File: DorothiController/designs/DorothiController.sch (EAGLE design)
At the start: 25 parts

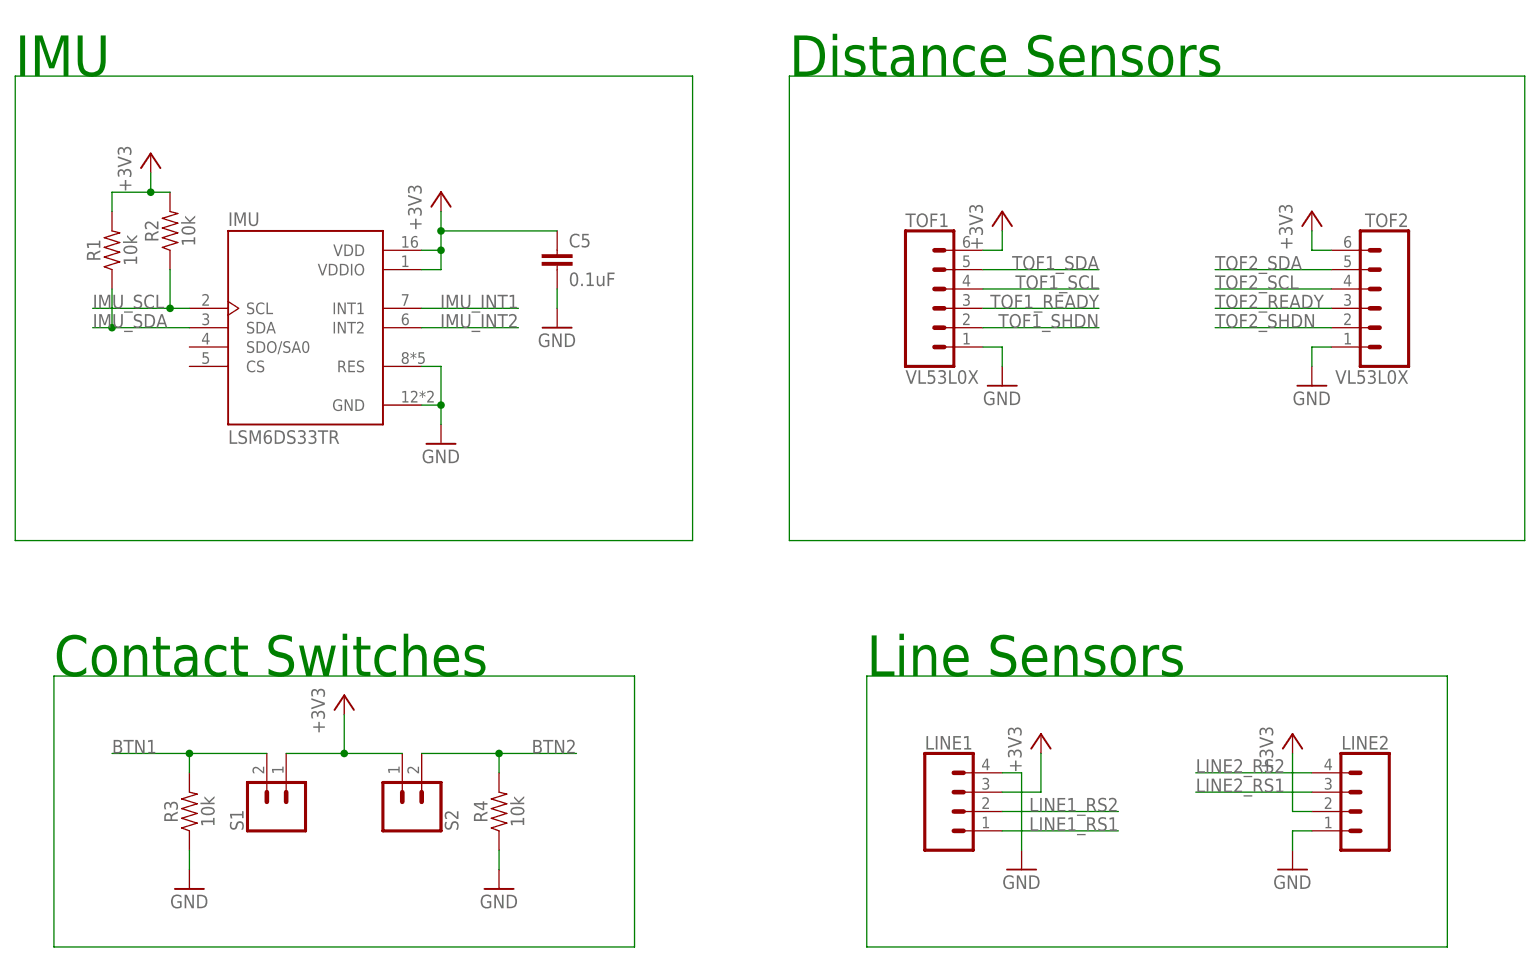
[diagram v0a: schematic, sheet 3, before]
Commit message: silk screen and status diode added
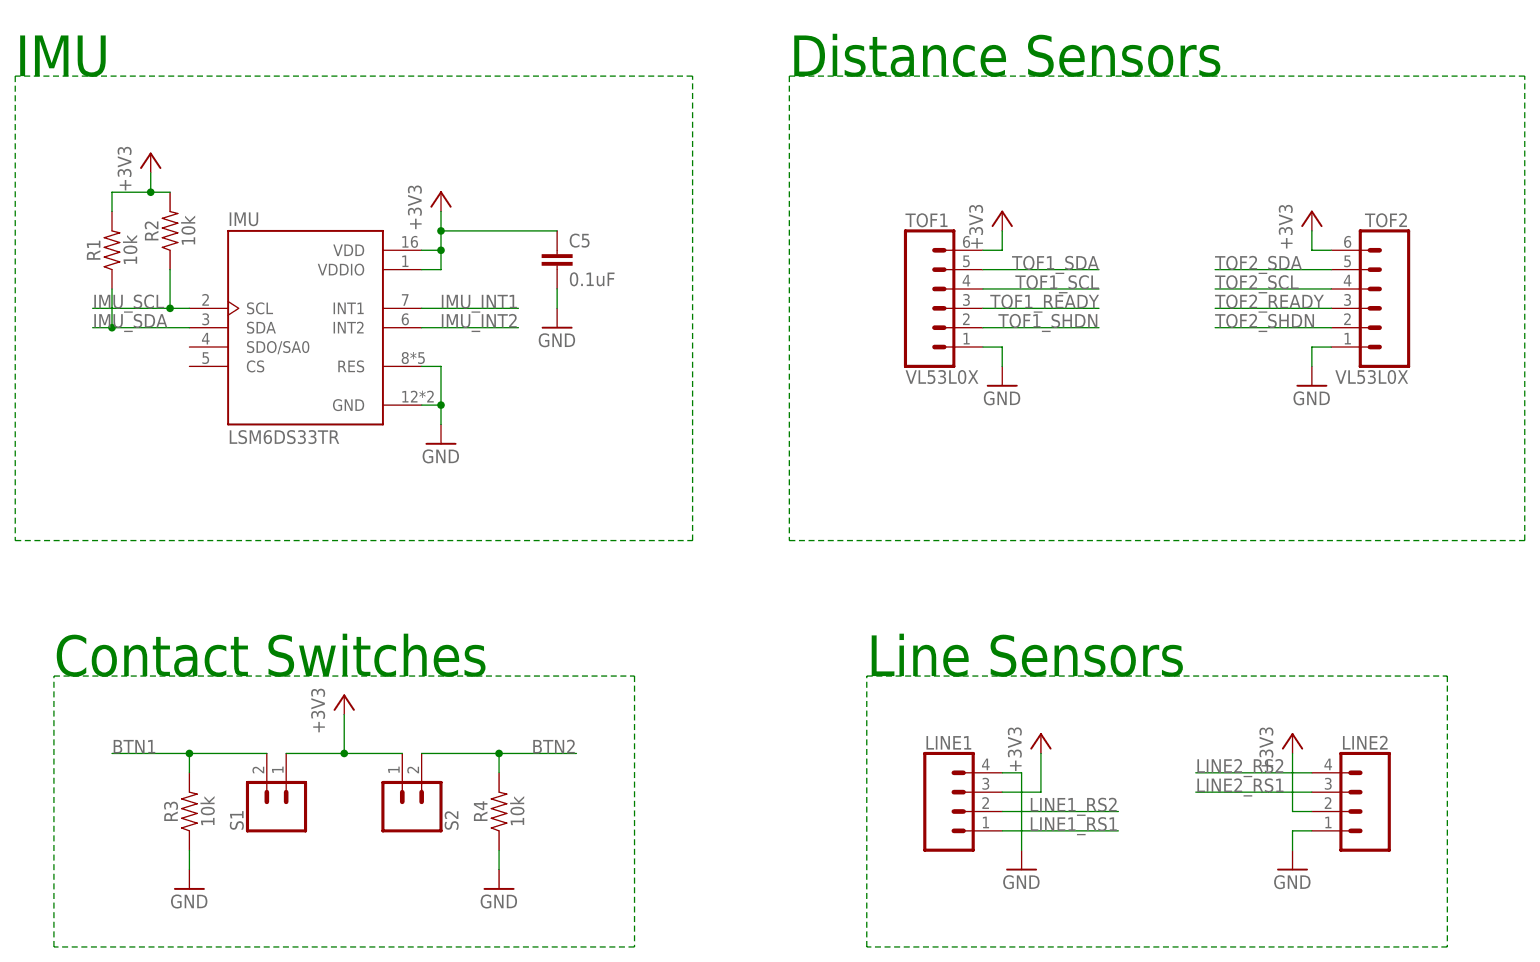
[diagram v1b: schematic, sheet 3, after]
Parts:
- added D1: (no value), SparkFun-LED:LED0603
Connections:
- new net INDICATOR: D1.A, U$1.23/A9/T/PWM
- net GND: now also D1.C

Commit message: forgot resistor
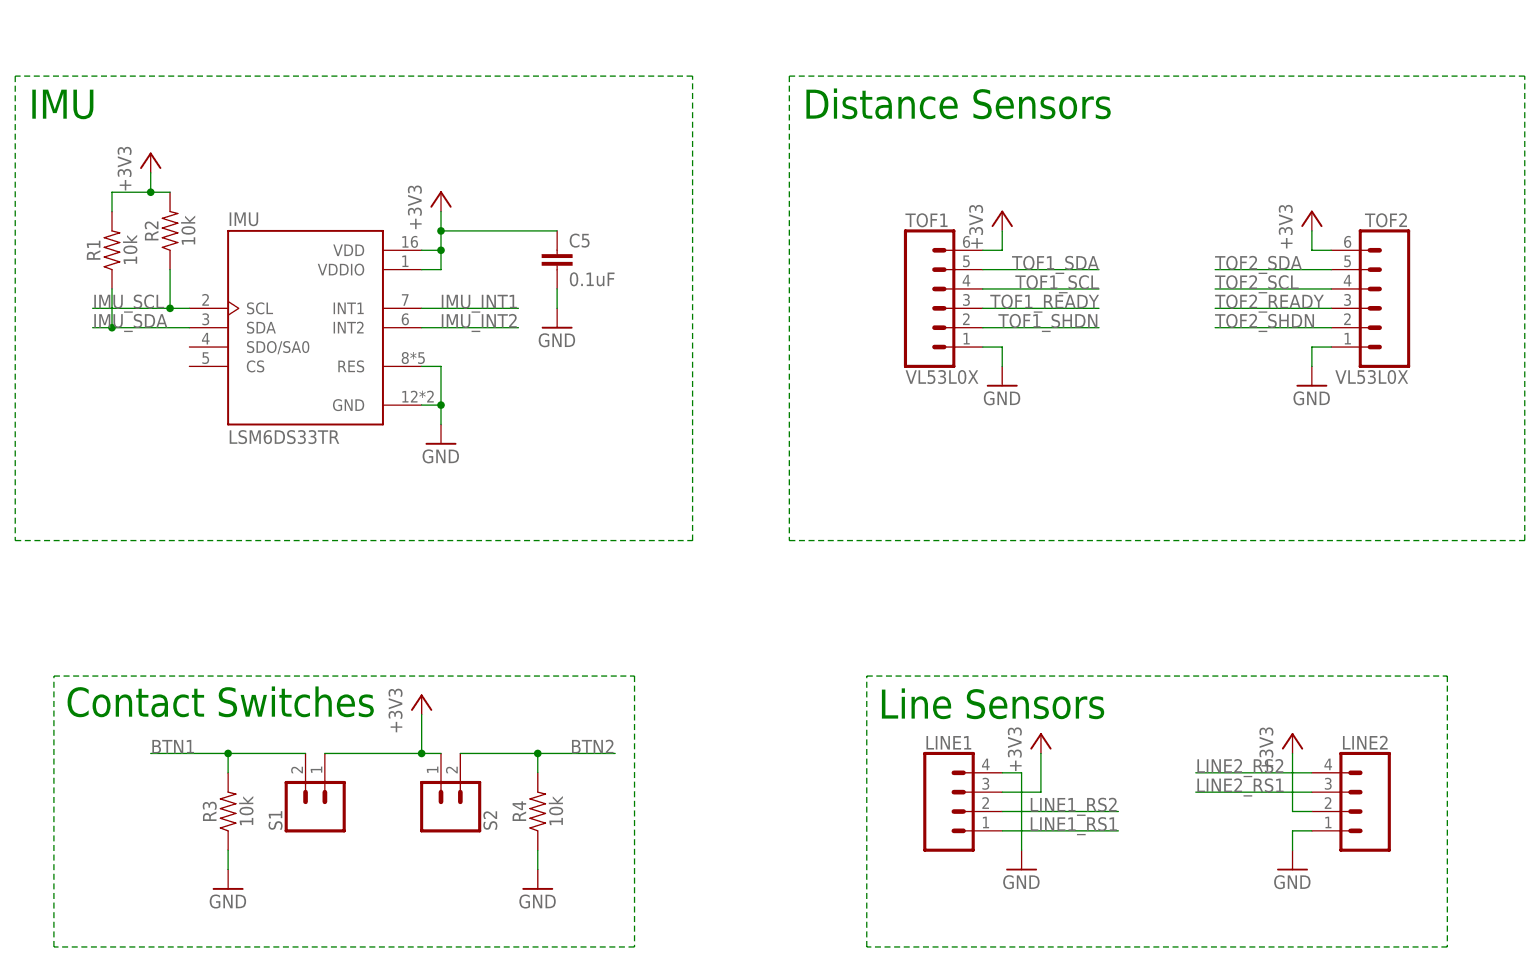
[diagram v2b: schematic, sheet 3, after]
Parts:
- added R5: 10k, SparkFun-Resistors:10KOHM-0603-1/10W-1%
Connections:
- new net N$5: D1.A, R5.1
- net INDICATOR: now also R5.2; no longer D1.A
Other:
- moved on the sheet: D1, R3, R4, S1, S2
